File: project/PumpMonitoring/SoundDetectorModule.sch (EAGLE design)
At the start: 33 parts, among them CN1 JST-PH-K*, IC1 LMV324

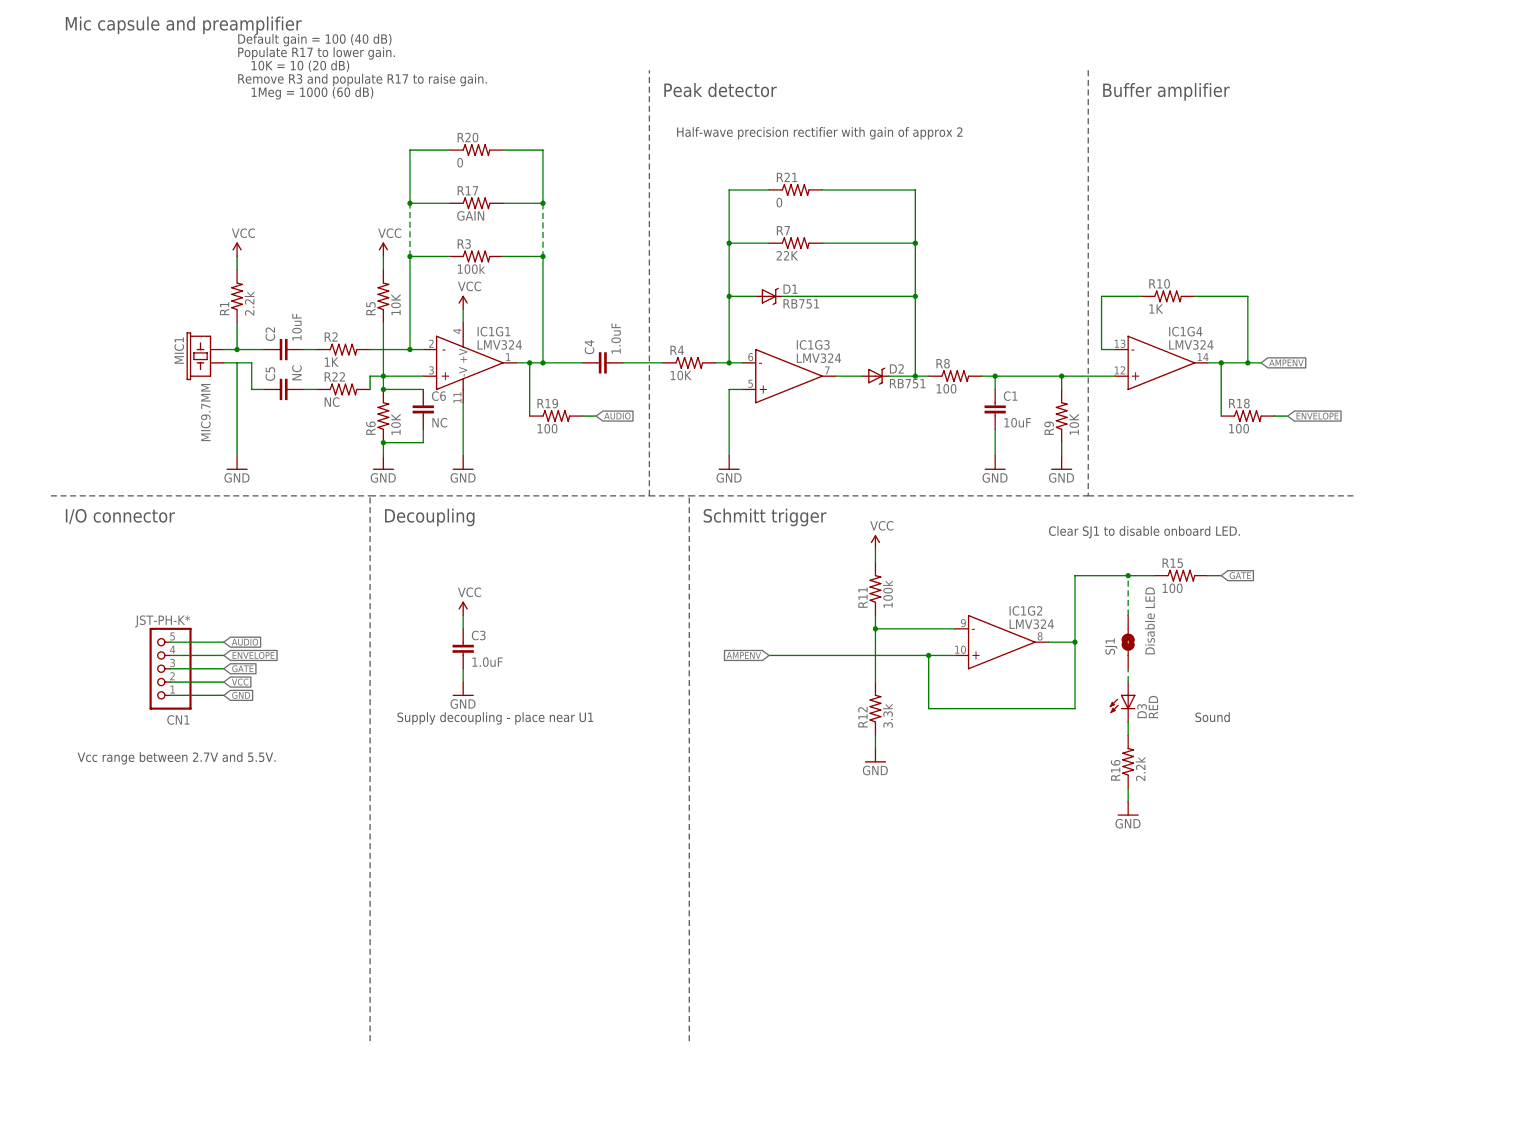
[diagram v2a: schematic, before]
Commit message: add ti.lbr and update motion/sound module
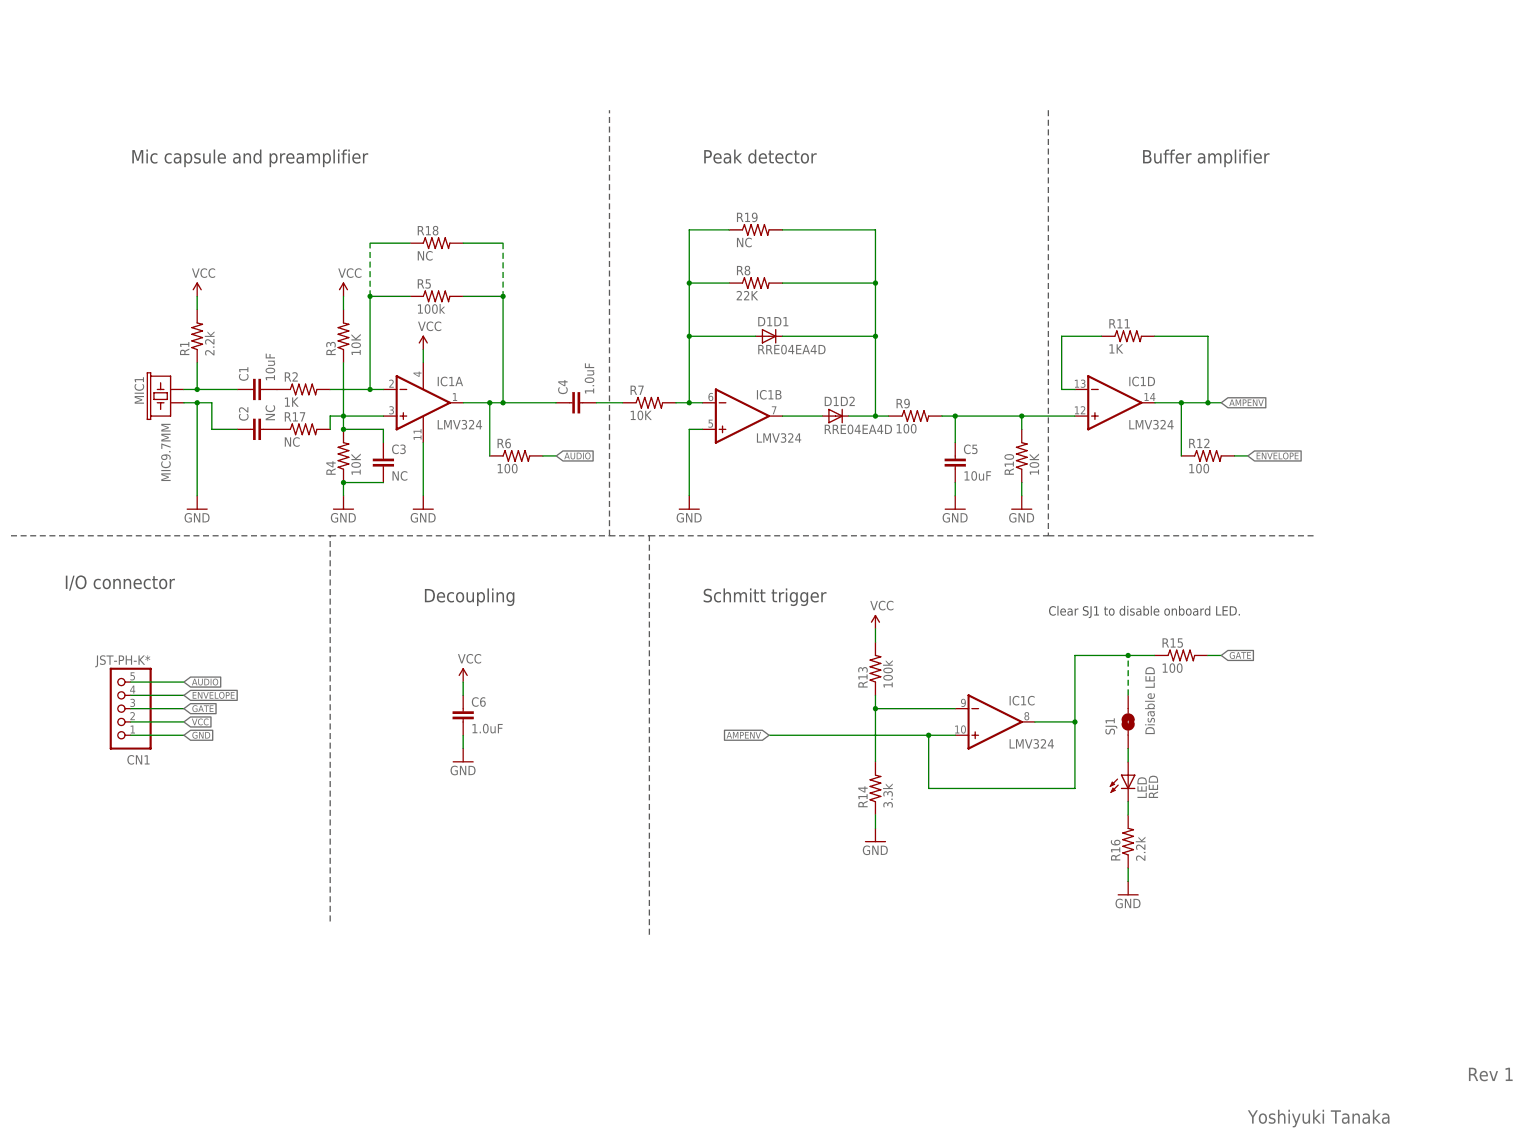
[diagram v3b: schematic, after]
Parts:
- removed D2: RB751, SparkFun-DiscreteSemi:RB751
- removed D3: RED, SparkFun-LED:LED-RED0603
- removed R20, R21: 0, resistor:R-US_0207/7
- removed R22: NC, SparkFun-Resistors:1KOHM1/10W1%(0603)
- added LED: RED, lazurite:SML-E1X
- added R13: 100k, rcl:R-US_R0603
- added R14: 3.3k, rcl:R-US_R0603
- C1: device SparkFun-Capacitors:10UF-6.3V-20%(1206) -> rcl:C-EUC1206
- C2: value 10uF -> NC; device SparkFun-Capacitors:10UF-6.3V-20%(1206) -> rcl:C-EUC0603
- C3: value 1.0uF -> NC; device SparkFun-Capacitors:1.0UF-16V-10%(0603) -> rcl:C-EUC0603
- C4: device SparkFun-Capacitors:1.0UF-16V-10%(0603) -> rcl:C-EUC0603
- C5: value NC -> 10uF; device SparkFun-Capacitors:1.0UF-16V-10%(0603) -> rcl:C-EUC1206
- C6: value NC -> 1.0uF; device SparkFun-Capacitors:1.0UF-16V-10%(0603) -> rcl:C-EUC0603
- D1: value RB751 -> RRE04EA4D; device SparkFun-DiscreteSemi:RB751 -> rohm2:RRE04EA4D
- IC1: device SparkFun-AnalogIC:LMV324 -> ti:LMV324
- R1, R16: device SparkFun-Resistors:2.2KOHM1/10W1%(0603) -> rcl:R-US_R0603
- R10: value 1K -> 10K; device SparkFun-Resistors:1KOHM1/10W1%(0603) -> rcl:R-US_R0603
- R11: value 100k -> 1K; device SparkFun-Resistors:100KOHM1/10W1%(0603) -> rcl:R-US_R0603
- R12: value 3.3k -> 100; device SparkFun-Resistors:3.3KOHM1/10W1%(0603) -> rcl:R-US_R0603
- R15: device SparkFun-Resistors:100OHM1/10W1%(0603) -> rcl:R-US_R0603
- R17: value GAIN -> NC; device SparkFun-Resistors:RESISTORPTH-1/4W-VERT-KIT -> rcl:R-US_R0603
- R18, R19: value 100 -> NC; device SparkFun-Resistors:100OHM1/10W1%(0603) -> resistor:R-US_0207/7
- R2: device SparkFun-Resistors:1KOHM1/10W1%(0603) -> rcl:R-US_R0603
- R3: value 100k -> 10K; device SparkFun-Resistors:100KOHM1/10W1%(0603) -> rcl:R-US_R0603
- R4: device SparkFun-Resistors:10KOHM1/10W1%(0603)0603 -> rcl:R-US_R0603
- R5: value 10K -> 100k; device SparkFun-Resistors:10KOHM1/10W1%(0603)0603 -> rcl:R-US_R0603
- R6, R9: value 10K -> 100; device SparkFun-Resistors:10KOHM1/10W1%(0603)0603 -> rcl:R-US_R0603
- R7: value 22K -> 10K; device SparkFun-Resistors:22KOHM1/10W1%(0603) -> rcl:R-US_R0603
- R8: value 100 -> 22K; device SparkFun-Resistors:100OHM1/10W1%(0603) -> rcl:R-US_R0603
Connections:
- net AMPENV: now also IC1C.+IN, IC1C.OUT, IC1D.OUT, R11.2, R12.1; no longer IC1G2.+IN, IC1G2.OUT, IC1G4.OUT, R10.2, R18.1
- net AUDIO: now also R6.2; no longer R19.2
- net ENVELOPE: now also R12.2; no longer R18.2
- net GND: now also C2.1, C5.2, IC1B.+IN, IC1P.V-, R10.1, R14.1, R4.1; no longer C1.2, C5.1, IC1G1.-V, IC1G3.+IN, R12.1, R6.1, R9.1
- net N$: now also IC1A.OUT, R18.2, R5.2, R6.1; no longer IC1G1.OUT, R17.2, R19.1, R20.2, R3.2
- net N$1: now also C1.1; no longer C2.1
- net N$10: now also C5.1, IC1D.+IN, R10.2; no longer C1.1, IC1G4.+IN, R8.2
- net N$11: now also IC1D.-IN, R11.1; no longer IC1G4.-IN, R10.1
- net N$12: now also LED.A; no longer D3.A
- net N$13: now also C2.2, R17.1; no longer C5.2, R22.1
- net N$15: now also IC1C.-IN, R13.1, R14.2; no longer IC1G2.-IN, R11.1, R12.2
- net N$2: now also C3.1, IC1A.+IN, R17.2, R3.1, R4.2; no longer C6.1, IC1G1.+IN, R22.2, R5.1, R6.2
- net N$3: now also LED.C; no longer D3.C
- net N$4: now also IC1A.-IN, R18.1, R5.1; no longer IC1G1.-IN, R17.1, R20.1, R3.1
- net N$5: now also C1.2; no longer C2.2
- net N$6: now also R7.1; no longer R4.1
- net N$7: now also D1D1.A, IC1B.-IN, R19.1, R7.2, R8.1; no longer D1.A, IC1G3.-IN, R21.1, R4.2, R7.1
- net N$8: now also D1D2.A, IC1B.OUT; no longer D2.A, IC1G3.OUT
- net N$9: now also D1D1.C, D1D2.C, R19.2, R8.2, R9.1; no longer D1.C, D2.C, R21.2, R7.2, R8.1
- net VCC: now also C6.1, IC1P.V+, R13.2, R3.2; no longer C3.1, IC1G1.+V, R11.2, R5.2
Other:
- note added: "Rev 1"
- note added: "Yoshiyuki Tanaka"
- note removed: "10K = 10 (20 dB)"
- note removed: "1Meg = 1000 (60 dB)"
- note removed: "Default gain = 100 (40 dB)"
- note removed: "Half-wave precision rectifier with gain of approx 2"
- note removed: "Populate R17 to lower gain."
- note removed: "Remove R3 and populate R17 to raise gain."
- note removed: "Sound"
- note removed: "Supply decoupling - place near U1"
- note removed: "Vcc range between 2.7V and 5.5V."
- moved on the sheet: C1, C2, C3, C4, C5, C6, CN1, MIC1, R1, R10, R11, R12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

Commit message: update project of pump monitoring incl. sound and motion.
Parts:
- added R20: 0, rcl:R-US_R0603
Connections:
- new net N$14: C2.1, MIC1.2, R20.2
- net GND: now also R20.1; no longer C2.1, MIC1.2
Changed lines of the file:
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@@
 <?xml version="1.0" encoding="utf-8"?>
 <!DOCTYPE eagle SYSTEM "eagle.dtd">
-<eagle version="7.7.0">
+<eagle version="7.6.0">
 <drawing>
 <settings>
@@
 <part name="D1" library="rohm2" deviceset="RRE04EA4D" device=""/>
 <part name="IC1" library="ti" deviceset="LMV324" device=""/>
+<part name="R20" library="rcl" deviceset="R-US_" device="R0603" value="0"/>
 </parts>
 <sheets>
@@
 <instance part="IC1" gate="C" x="254" y="88.9"/>
 <instance part="IC1" gate="D" x="276.86" y="149.86"/>
+<instance part="R20" gate="G$1" x="101.6" y="139.7" rot="R90"/>
 </instances>
 <busses>
@@
 </segment>
 <segment>
-<pinref part="MIC1" gate="G$1" pin="2"/>
-<wire x1="99.06" y1="149.86" x2="101.6" y2="149.86" width="0.1524" layer="91"/>
 <pinref part="GND2" gate="1" pin="GND"/>
-<wire x1="101.6" y1="149.86" x2="101.6" y2="132.08" width="0.1524" layer="91"/>
-<wire x1="101.6" y1="149.86" x2="104.394" y2="149.86" width="0.1524" layer="91"/>
-<wire x1="104.394" y1="149.86" x2="104.394" y2="144.78" width="0.1524" layer="91"/>
-<wire x1="104.394" y1="144.78" x2="109.22" y2="144.78" width="0.1524" layer="91"/>
-<pinref part="C2" gate="G$1" pin="1"/>
-<junction x="101.6" y="149.86"/>
+<pinref part="R20" gate="G$1" pin="1"/>
+<wire x1="101.6" y1="134.62" x2="101.6" y2="132.08" width="0.1524" layer="91"/>
 </segment>
 <segment>
@@
 </segment>
 </net>
+<net name="N$14" class="0">
+<segment>
+<pinref part="MIC1" gate="G$1" pin="2"/>
+<wire x1="99.06" y1="149.86" x2="101.6" y2="149.86" width="0.1524" layer="91"/>
+<wire x1="101.6" y1="149.86" x2="101.6" y2="144.78" width="0.1524" layer="91"/>
+<wire x1="101.6" y1="149.86" x2="104.394" y2="149.86" width="0.1524" layer="91"/>
+<wire x1="104.394" y1="149.86" x2="104.394" y2="144.78" width="0.1524" layer="91"/>
+<wire x1="104.394" y1="144.78" x2="109.22" y2="144.78" width="0.1524" layer="91"/>
+<pinref part="C2" gate="G$1" pin="1"/>
+<junction x="101.6" y="149.86"/>
+<pinref part="R20" gate="G$1" pin="2"/>
+</segment>
+</net>
